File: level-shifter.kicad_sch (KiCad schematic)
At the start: 2 parts, among them U8 SN74LV1T125DBV

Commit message: schem: add title
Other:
- company: (none) -> Rémi Ait-Younes
- title: (none) -> RPI CAN FD Power Hat+
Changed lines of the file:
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@@
 	(generator_version "10.0")
 	(paper "A4")
+	(title_block
+		(title "RPI CAN FD Power Hat+")
+		(date "2026-04-11")
+		(rev "01")
+		(company "Rémi Ait-Younes")
+	)
 	(junction
 		(at 135.89 86.36)

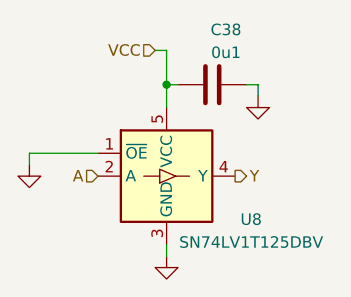
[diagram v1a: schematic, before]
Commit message: schem: renumber
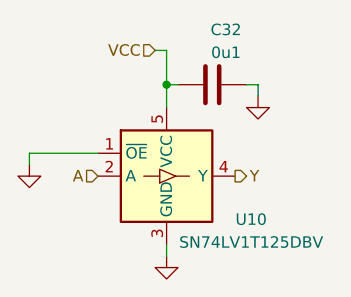
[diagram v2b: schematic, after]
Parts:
- renumbered C38 to C32, U8 to U10
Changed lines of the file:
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@@
 		(dnp no)
 		(fields_autoplaced yes)
-		(property "Reference" "#PWR07"
+		(property "Reference" "#PWR076"
 			(at 135.89 111.76 0)
 			(hide yes)
@@
 			(project "rpi-canfd-pwr-hat"
 				(path "/35b6363d-fbe9-4c33-b2ab-05d20bd8dec5/0ffe3062-0220-4f4c-9e1b-ebaed8d5ff8b"
-					(reference "#PWR09")
+					(reference "#PWR079")
 					(unit 1)
 				)
 				(path "/35b6363d-fbe9-4c33-b2ab-05d20bd8dec5/511c840a-a9c9-4605-941b-9bd54be2269f"
-					(reference "#PWR012")
+					(reference "#PWR082")
 					(unit 1)
 				)
 				(path "/35b6363d-fbe9-4c33-b2ab-05d20bd8dec5/9a7ae9d6-f6f6-42a5-9e1a-d003001c9638"
-					(reference "#PWR07")
+					(reference "#PWR076")
 					(unit 1)
 				)
 				(path "/35b6363d-fbe9-4c33-b2ab-05d20bd8dec5/da2c2396-5230-4041-87ba-74d9472c7a1e"
-					(reference "#PWR015")
+					(reference "#PWR085")
 					(unit 1)
 				)
@@
 		(in_pos_files yes)
 		(dnp no)
-		(property "Reference" "C38"
+		(property "Reference" "C32"
 			(at 142.494 80.264 90)
 			(show_name no)
@@
 			(project "rpi-canfd-pwr-hat"
 				(path "/35b6363d-fbe9-4c33-b2ab-05d20bd8dec5/0ffe3062-0220-4f4c-9e1b-ebaed8d5ff8b"
-					(reference "C39")
+					(reference "C33")
 					(unit 1)
 				)
 				(path "/35b6363d-fbe9-4c33-b2ab-05d20bd8dec5/511c840a-a9c9-4605-941b-9bd54be2269f"
-					(reference "C40")
+					(reference "C34")
 					(unit 1)
 				)
 				(path "/35b6363d-fbe9-4c33-b2ab-05d20bd8dec5/9a7ae9d6-f6f6-42a5-9e1a-d003001c9638"
-					(reference "C38")
+					(reference "C32")
 					(unit 1)
 				)
 				(path "/35b6363d-fbe9-4c33-b2ab-05d20bd8dec5/da2c2396-5230-4041-87ba-74d9472c7a1e"
-					(reference "C41")
+					(reference "C35")
 					(unit 1)
 				)
@@
 		(dnp no)
 		(fields_autoplaced yes)
-		(property "Reference" "#PWR05"
+		(property "Reference" "#PWR075"
 			(at 120.65 101.6 0)
 			(hide yes)
@@
 			(project "rpi-canfd-pwr-hat"
 				(path "/35b6363d-fbe9-4c33-b2ab-05d20bd8dec5/0ffe3062-0220-4f4c-9e1b-ebaed8d5ff8b"
-					(reference "#PWR08")
+					(reference "#PWR078")
 					(unit 1)
 				)
 				(path "/35b6363d-fbe9-4c33-b2ab-05d20bd8dec5/511c840a-a9c9-4605-941b-9bd54be2269f"
-					(reference "#PWR011")
+					(reference "#PWR081")
 					(unit 1)
 				)
 				(path "/35b6363d-fbe9-4c33-b2ab-05d20bd8dec5/9a7ae9d6-f6f6-42a5-9e1a-d003001c9638"
-					(reference "#PWR05")
+					(reference "#PWR075")
 					(unit 1)
 				)
 				(path "/35b6363d-fbe9-4c33-b2ab-05d20bd8dec5/da2c2396-5230-4041-87ba-74d9472c7a1e"
-					(reference "#PWR014")
+					(reference "#PWR084")
 					(unit 1)
 				)
@@
 		(in_pos_files yes)
 		(dnp no)
-		(property "Reference" "U8"
+		(property "Reference" "U10"
 			(at 145.288 101.346 0)
 			(show_name no)
@@
 			(project "rpi-canfd-pwr-hat"
 				(path "/35b6363d-fbe9-4c33-b2ab-05d20bd8dec5/0ffe3062-0220-4f4c-9e1b-ebaed8d5ff8b"
-					(reference "U9")
+					(reference "U11")
 					(unit 1)
 				)
 				(path "/35b6363d-fbe9-4c33-b2ab-05d20bd8dec5/511c840a-a9c9-4605-941b-9bd54be2269f"
+					(reference "U12")
+					(unit 1)
+				)
+				(path "/35b6363d-fbe9-4c33-b2ab-05d20bd8dec5/9a7ae9d6-f6f6-42a5-9e1a-d003001c9638"
 					(reference "U10")
 					(unit 1)
 				)
-				(path "/35b6363d-fbe9-4c33-b2ab-05d20bd8dec5/9a7ae9d6-f6f6-42a5-9e1a-d003001c9638"
-					(reference "U8")
-					(unit 1)
-				)
 				(path "/35b6363d-fbe9-4c33-b2ab-05d20bd8dec5/da2c2396-5230-4041-87ba-74d9472c7a1e"
-					(reference "U11")
+					(reference "U13")
 					(unit 1)
 				)
@@
 		(dnp no)
 		(fields_autoplaced yes)
-		(property "Reference" "#PWR06"
+		(property "Reference" "#PWR077"
 			(at 146.05 93.98 0)
 			(hide yes)
@@
 			(project "rpi-canfd-pwr-hat"
 				(path "/35b6363d-fbe9-4c33-b2ab-05d20bd8dec5/0ffe3062-0220-4f4c-9e1b-ebaed8d5ff8b"
-					(reference "#PWR010")
+					(reference "#PWR080")
 					(unit 1)
 				)
 				(path "/35b6363d-fbe9-4c33-b2ab-05d20bd8dec5/511c840a-a9c9-4605-941b-9bd54be2269f"
-					(reference "#PWR013")
+					(reference "#PWR083")
 					(unit 1)
 				)
 				(path "/35b6363d-fbe9-4c33-b2ab-05d20bd8dec5/9a7ae9d6-f6f6-42a5-9e1a-d003001c9638"
-					(reference "#PWR06")
+					(reference "#PWR077")
 					(unit 1)
 				)
 				(path "/35b6363d-fbe9-4c33-b2ab-05d20bd8dec5/da2c2396-5230-4041-87ba-74d9472c7a1e"
-					(reference "#PWR016")
-					(unit 1)
-				)
+					(reference "#PWR086")
+					(unit 1)
+				)
